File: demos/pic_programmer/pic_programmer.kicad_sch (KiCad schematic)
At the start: 59 parts

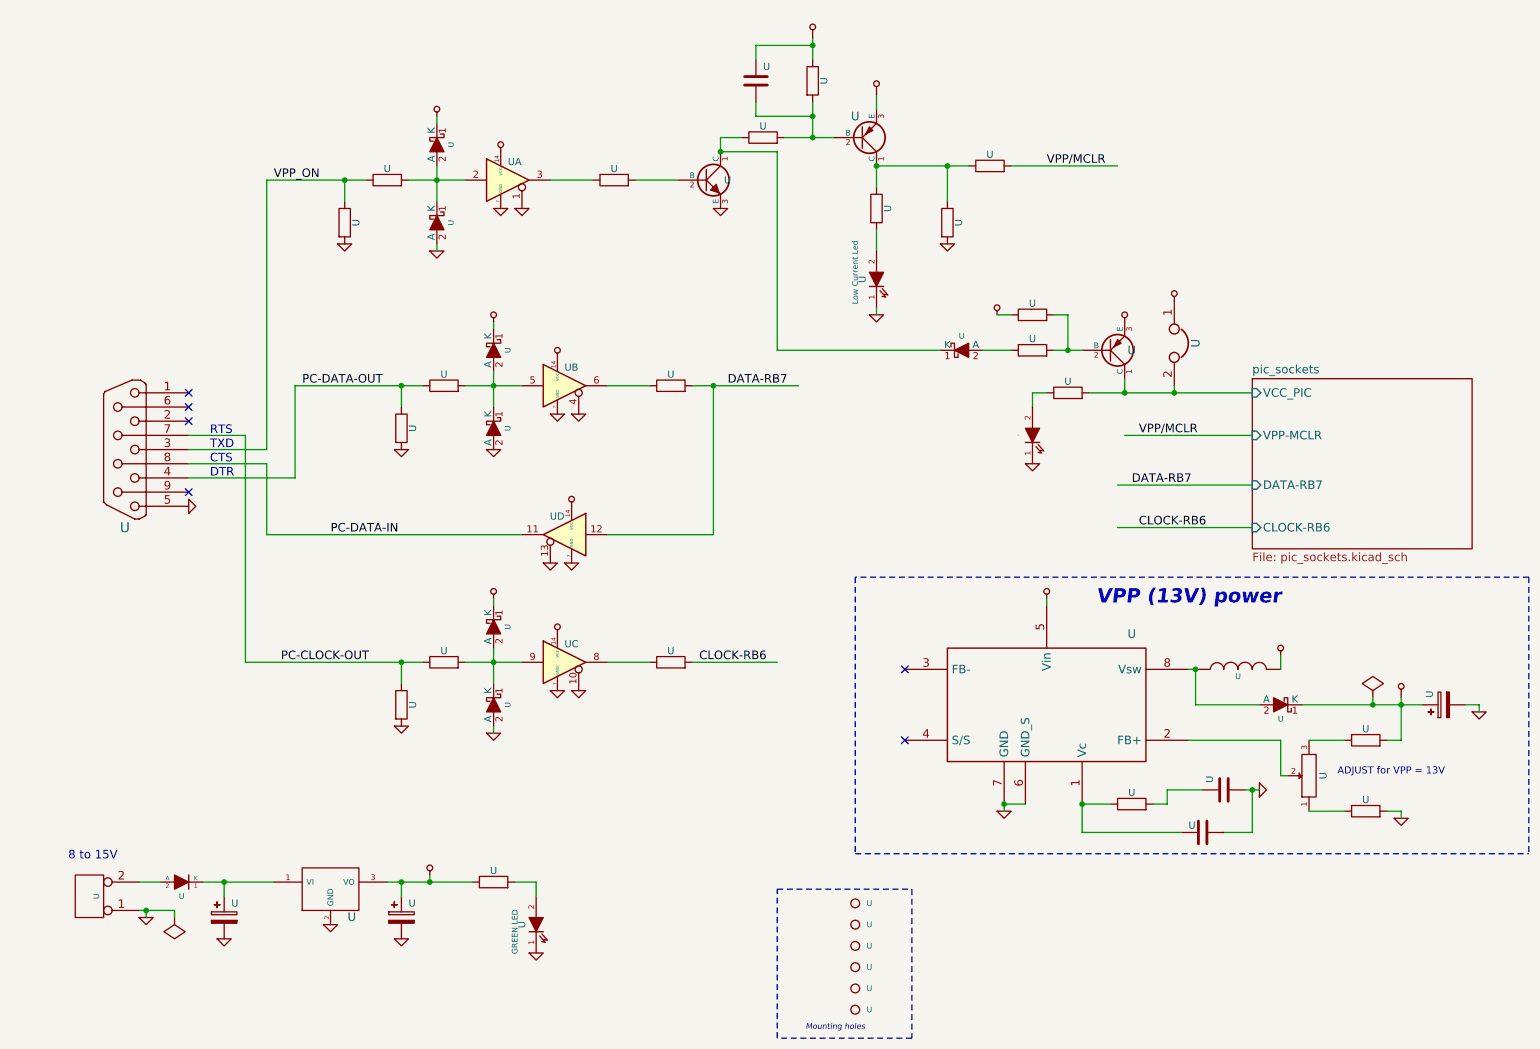
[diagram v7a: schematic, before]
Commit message: Update demos using latest file formats.
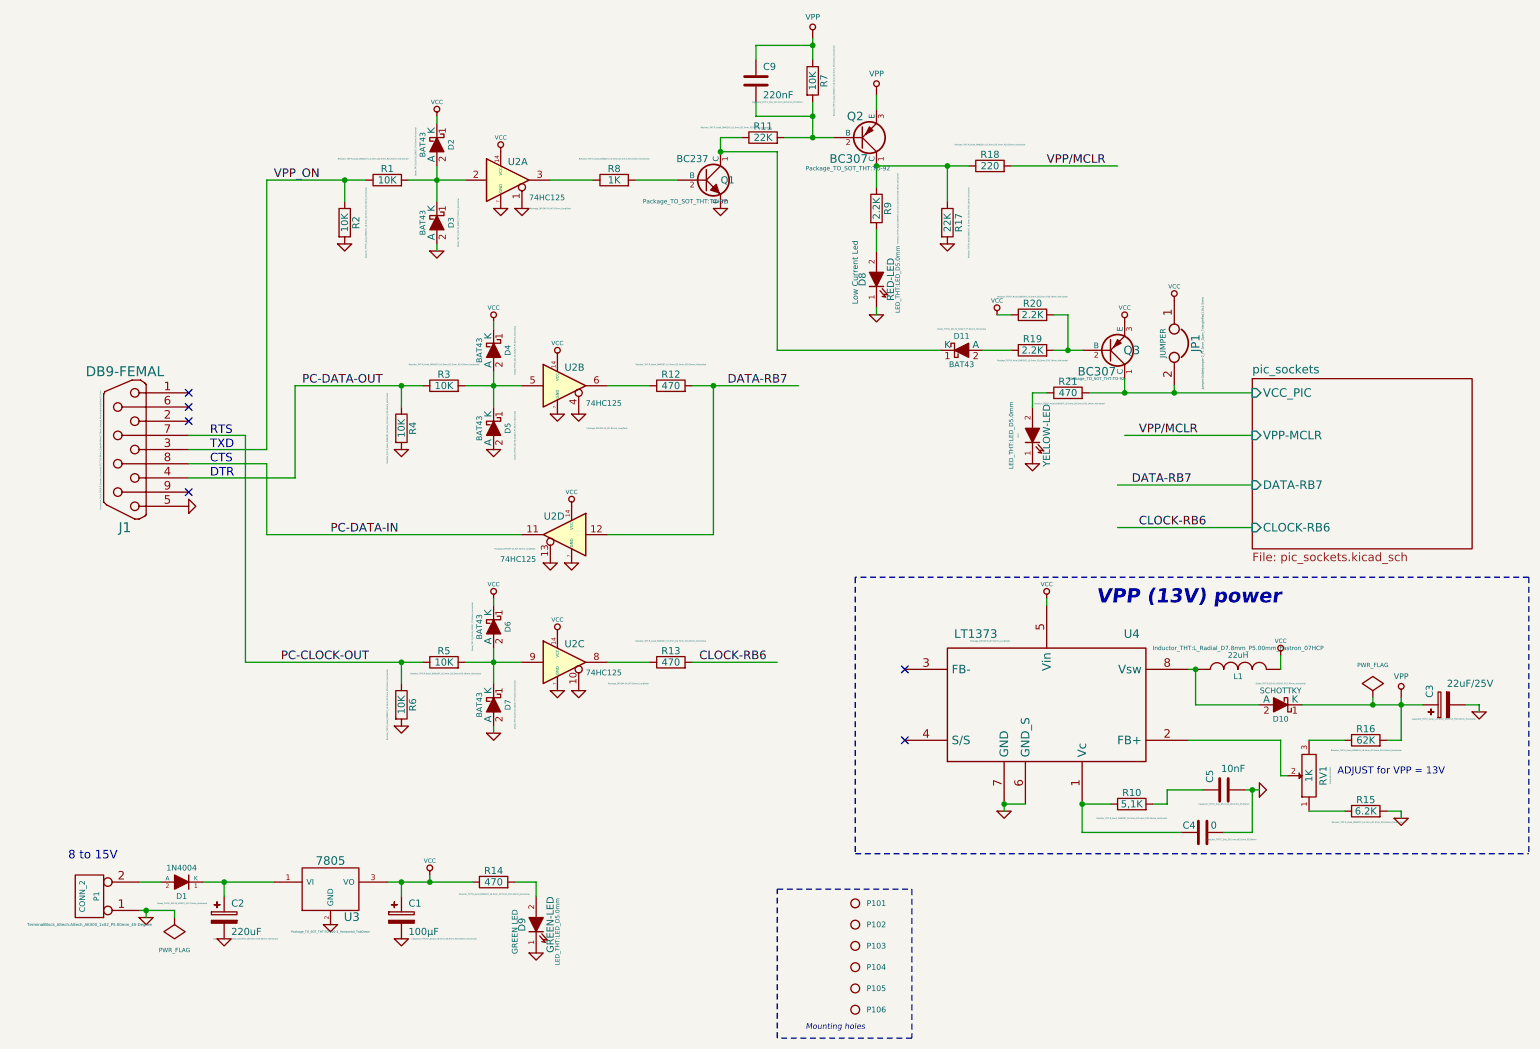
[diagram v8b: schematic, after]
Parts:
- removed U (x3): (no value), symbol pic_programmer_schlib:VPP
- C1: renamed from U; value (none) -> 100µF; footprint (none) -> Capacitor_THT:CP_Axial_L18.0mm_D6.5mm_P25.00mm_Horizontal
- C2: renamed from U; value (none) -> 220uF; footprint (none) -> Capacitor_THT:CP_Axial_L18.0mm_D6.5mm_P25.00mm_Horizontal
- C3: renamed from U; value (none) -> 22uF/25V; footprint (none) -> Capacitor_THT:C_Axial_L12.0mm_D6.5mm_P20.00mm_Horizontal
- C4: renamed from U; value (none) -> 0; footprint (none) -> Capacitor_THT:C_Disc_D5.1mm_W3.2mm_P5.00mm
- C5: renamed from U; value (none) -> 10nF; footprint (none) -> Capacitor_THT:C_Disc_D5.1mm_W3.2mm_P5.00mm
- C9: renamed from U; value (none) -> 220nF; footprint (none) -> Capacitor_THT:C_Disc_D5.1mm_W3.2mm_P5.00mm
- D1: renamed from U; value (none) -> 1N4004; footprint (none) -> Diode_THT:D_DO-35_SOD27_P12.70mm_Horizontal
- D10: renamed from U; value (none) -> SCHOTTKY; footprint (none) -> Diode_THT:D_DO-35_SOD27_P12.70mm_Horizontal
- D11, D2, D3, D4, D5, D6, D7: renamed from U; value (none) -> BAT43; footprint (none) -> Diode_THT:D_DO-35_SOD27_P7.62mm_Horizontal
- D12: renamed from U; value (none) -> YELLOW-LED; footprint (none) -> LED_THT:LED_D5.0mm
- D8: renamed from U; value (none) -> RED-LED; footprint (none) -> LED_THT:LED_D5.0mm
- D9: renamed from U; value (none) -> GREEN-LED; footprint (none) -> LED_THT:LED_D5.0mm
- J1: renamed from U; value (none) -> DB9-FEMAL; footprint (none) -> Connector_Dsub:DSUB-9_Female_Horizontal_P2.77x2.84mm_EdgePinOffset7.70mm_Housed_MountingHolesOffset9.12mm
- JP1: renamed from U; value (none) -> JUMPER; footprint (none) -> Jumper:SolderJumper-2_P1.3mm_Open_TrianglePad1.0x1.5mm
- L1: renamed from U; value (none) -> 22uH; footprint (none) -> Inductor_THT:L_Radial_D7.8mm_P5.00mm_Fastron_07HCP
- P1: renamed from U; value (none) -> CONN_2; footprint (none) -> TerminalBlock_Altech:Altech_AK300_1x02_P5.00mm_45-Degree
- P101, P102, P103, P104, P105, P106: renamed from U; value (none) -> CONN_1; footprint (none) -> MountingHole:MountingHole_4.3mm_M4
- Q1: renamed from U; value (none) -> BC237; footprint (none) -> Package_TO_SOT_THT:TO-92
- Q2, Q3: renamed from U; value (none) -> BC307; footprint (none) -> Package_TO_SOT_THT:TO-92
- R1, R2, R3, R4, R5, R6, R7: renamed from U; value (none) -> 10K; footprint (none) -> Resistor_THT:R_Axial_DIN0207_L6.3mm_D2.5mm_P10.16mm_Horizontal
- R10: renamed from U; value (none) -> 5,1K; footprint (none) -> Resistor_THT:R_Axial_DIN0207_L6.3mm_D2.5mm_P10.16mm_Horizontal
- R11, R17: renamed from U; value (none) -> 22K; footprint (none) -> Resistor_THT:R_Axial_DIN0207_L6.3mm_D2.5mm_P10.16mm_Horizontal
- R12, R13, R14, R21: renamed from U; value (none) -> 470; footprint (none) -> Resistor_THT:R_Axial_DIN0207_L6.3mm_D2.5mm_P10.16mm_Horizontal
- R15: renamed from U; value (none) -> 6.2K; footprint (none) -> Resistor_THT:R_Axial_DIN0207_L6.3mm_D2.5mm_P10.16mm_Horizontal
- R16: renamed from U; value (none) -> 62K; footprint (none) -> Resistor_THT:R_Axial_DIN0207_L6.3mm_D2.5mm_P10.16mm_Horizontal
- R18: renamed from U; value (none) -> 220; footprint (none) -> Resistor_THT:R_Axial_DIN0207_L6.3mm_D2.5mm_P10.16mm_Horizontal
- R19, R20, R9: renamed from U; value (none) -> 2.2K; footprint (none) -> Resistor_THT:R_Axial_DIN0207_L6.3mm_D2.5mm_P10.16mm_Horizontal
- R8: renamed from U; value (none) -> 1K; footprint (none) -> Resistor_THT:R_Axial_DIN0207_L6.3mm_D2.5mm_P10.16mm_Horizontal
- RV1: renamed from U; value (none) -> 1K; footprint (none) -> footprints:RV2X4
- U2: renamed from U; value (none) -> 74HC125; footprint (none) -> Package_DIP:DIP-14_W7.62mm_LongPads
- U3: renamed from U; value (none) -> 7805; footprint (none) -> Package_TO_SOT_THT:TO-220-3_Horizontal_TabDown
- U4: renamed from U; value (none) -> LT1373; footprint (none) -> Package_DIP:DIP-8_W7.62mm_LongPads
